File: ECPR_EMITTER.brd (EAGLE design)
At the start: 66 x 95 mm, 22 parts, among them IC1 78L05, IC2 ATMEGA8-PU, J1 0802_SCREEN, Q1 BFR96, U1 AD9850 DDS Module

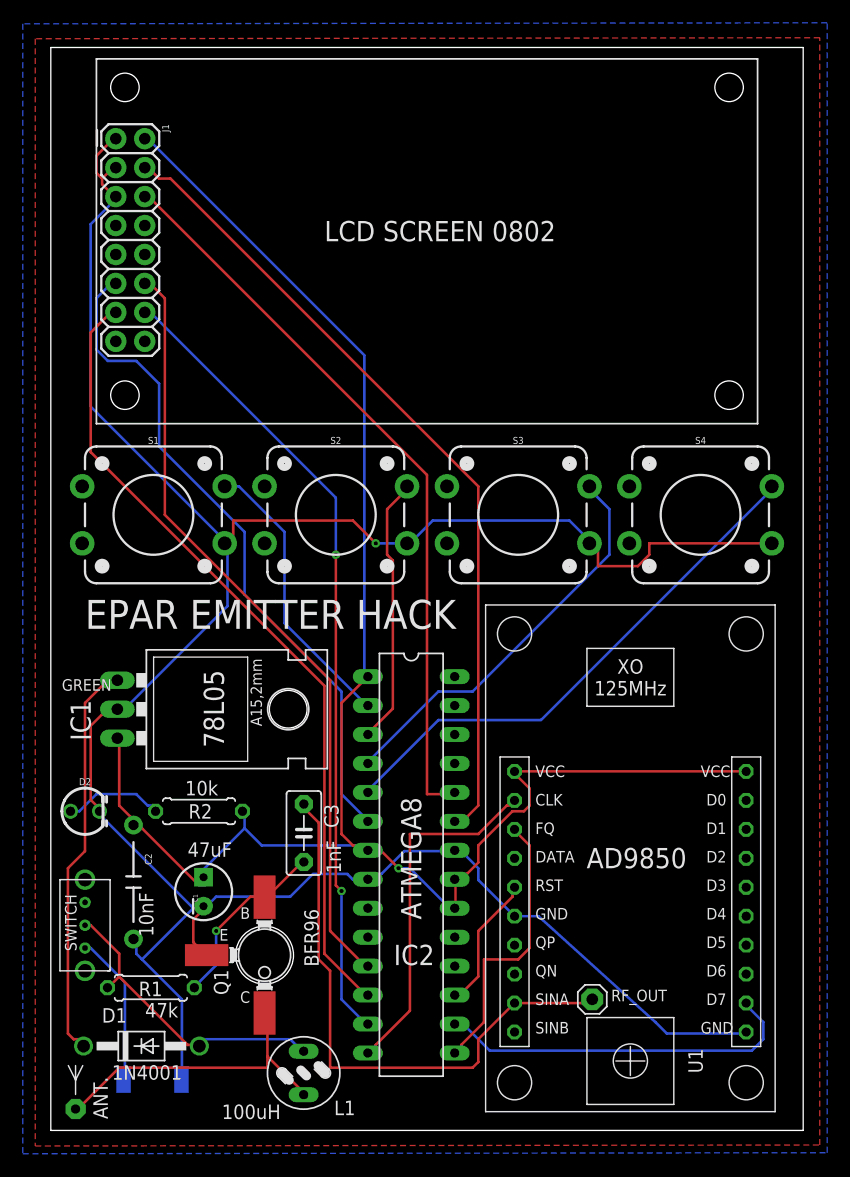
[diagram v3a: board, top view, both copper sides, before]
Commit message: feat(pcb): add rounded corners to the pcb
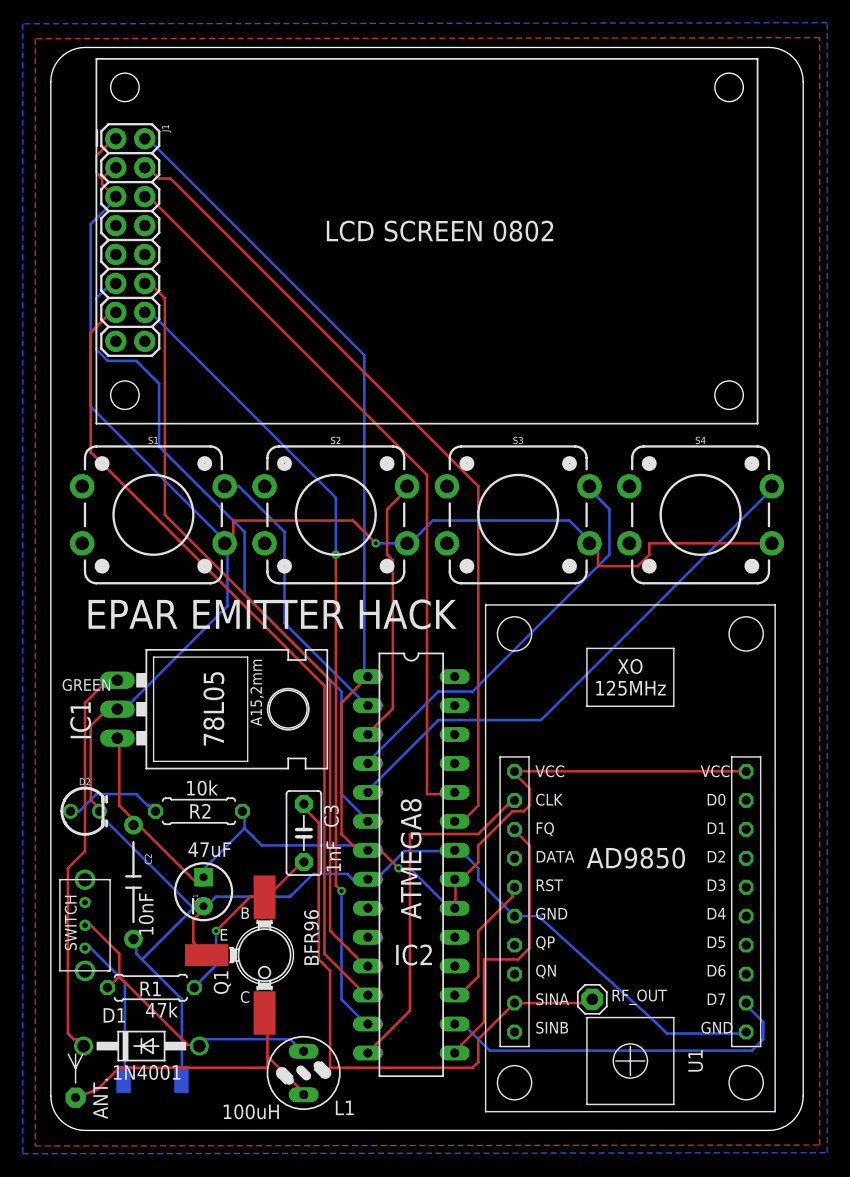
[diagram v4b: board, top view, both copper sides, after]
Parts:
- moved U$1 1.00 mm to (2.17, 2.88)
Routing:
- net N$7: track 27.8 -> 27.3 mm
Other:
- outline, holes or cut-outs redrawn
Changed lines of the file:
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@@
 <layer number="43" name="vRestrict" color="2" fill="10" visible="no" active="yes"/>
 <layer number="44" name="Drills" color="7" fill="1" visible="no" active="yes"/>
-<layer number="45" name="Holes" color="7" fill="1" visible="no" active="yes"/>
+<layer number="45" name="Holes" color="7" fill="1" visible="yes" active="yes"/>
 <layer number="46" name="Milling" color="3" fill="1" visible="no" active="yes"/>
 <layer number="47" name="Measures" color="7" fill="1" visible="no" active="yes"/>
@@
 <board>
 <plain>
-<wire x1="0" y1="0" x2="66" y2="0" width="0" layer="20"/>
-<wire x1="66" y1="0" x2="66" y2="95" width="0" layer="20"/>
-<wire x1="66" y1="95" x2="0" y2="95" width="0" layer="20"/>
-<wire x1="0" y1="95" x2="0" y2="0" width="0" layer="20"/>
 <dimension x1="4" y1="94" x2="62" y2="94" x3="33" y3="94" textsize="1.778" layer="51"/>
 <dimension x1="62" y1="94" x2="62" y2="62" x3="62" y3="78" textsize="1.778" layer="51"/>
@@
 <text x="57.5" y="28.5" size="1.016" layer="21">D0</text>
 <text x="57" y="31" size="1.016" layer="21">VCC</text>
+<wire x1="0" y1="92" x2="0" y2="3" width="0" layer="20"/>
+<wire x1="0" y1="3" x2="3" y2="0" width="0" layer="20" curve="90"/>
+<wire x1="63" y1="0" x2="66" y2="3" width="0" layer="20" curve="90"/>
+<wire x1="66" y1="3" x2="66" y2="92" width="0" layer="20"/>
+<wire x1="66" y1="92" x2="63" y2="95" width="0" layer="20" curve="90"/>
+<wire x1="63" y1="95" x2="3" y2="95" width="0" layer="20"/>
+<wire x1="3" y1="95" x2="0" y2="92" width="0" layer="20" curve="90"/>
+<wire x1="3" y1="0" x2="63" y2="0" width="0" layer="20"/>
 </plain>
 <attributes>
@@
 <attribute name="VALUE" x="57" y="47.777" size="0.6096" layer="27" font="vector" ratio="20" align="top-center"/>
 </element>
-<element name="U$1" library="computronics.com.au" package="ANTENNA" value="ANT." x="2.17" y="1.88" smashed="yes"/>
+<element name="U$1" library="computronics.com.au" package="ANTENNA" value="ANT." x="2.17" y="2.88" smashed="yes"/>
 <element name="L1" library="inductors" package="82114R" value="82114R" x="22.18" y="5.04" smashed="yes" rot="R180">
 <attribute name="NAME" x="26.72" y="2.611" size="1.27" layer="25" ratio="10" rot="R180"/>
@@
 <wire x1="22" y1="3.5" x2="22.18" y2="3.135" width="0.2286" layer="1"/>
 <wire x1="19" y1="10" x2="18.75" y2="10.3" width="0.2286" layer="1"/>
-<wire x1="6" y1="5.5" x2="2.5" y2="2" width="0.2286" layer="1"/>
+<wire x1="6" y1="5.5" x2="4.071428125" y2="3.571428125" width="0.2286" layer="1"/>
 <wire x1="19" y1="5.5" x2="6" y2="5.5" width="0.2286" layer="1"/>
 <wire x1="19" y1="6.5" x2="19" y2="5.5" width="0.2286" layer="1"/>
-<wire x1="2.5" y1="2" x2="2.17" y2="1.88" width="0.2286" layer="1"/>
+<wire x1="4.071428125" y1="3.571428125" x2="2.17" y2="2.88" width="0.2286" layer="1"/>
 </signal>
 <signal name="N$8">

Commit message: fix: screen orientation & pin23/24
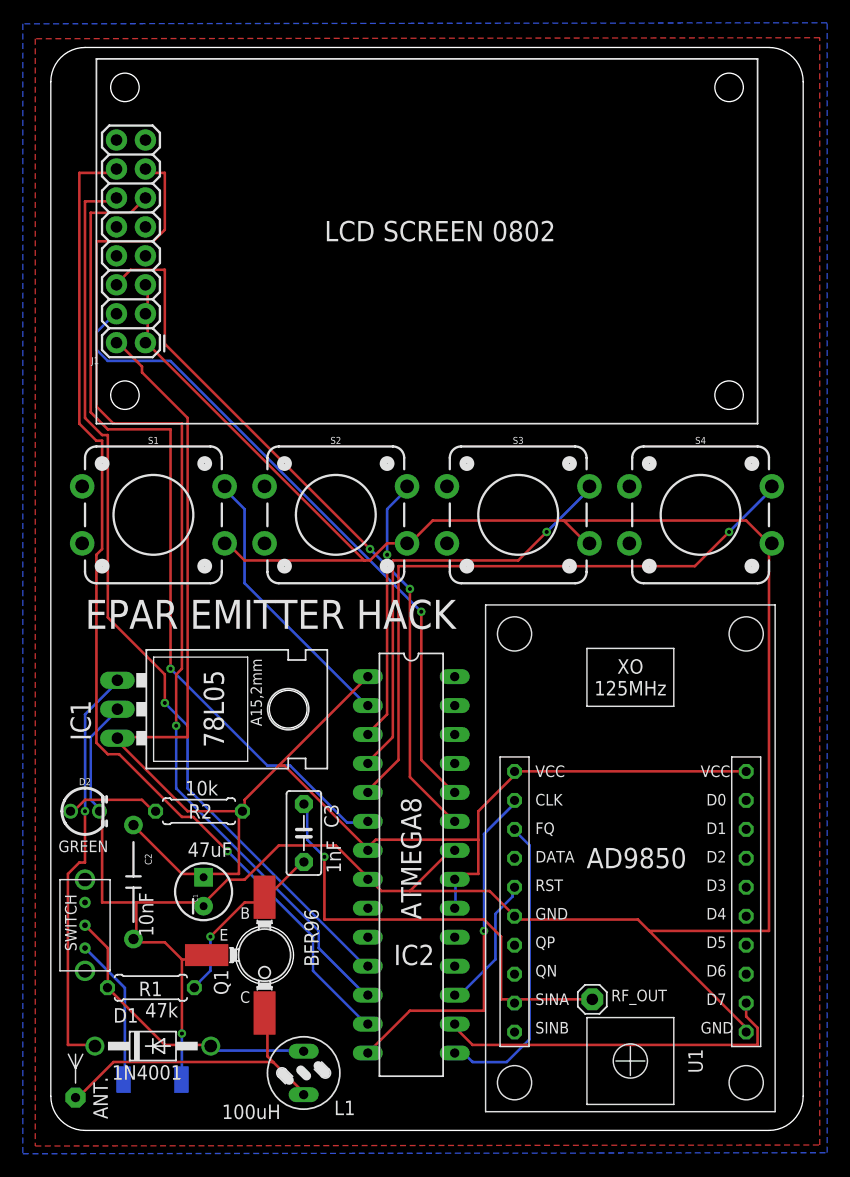
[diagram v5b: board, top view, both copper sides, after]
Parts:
- moved J1 18.1 mm to (8.30, 69.1), turned to 90 degrees
- moved D1 1.00 mm to (8.95, 7.40)
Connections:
- net N$8: now also IC2.24; no longer IC2.23
- net N$9: now also IC2.23; no longer IC2.24
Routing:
- net N$13: track 71.4 -> 93.3 mm, vias 0 -> 1
- net N$10: track 71.1 -> 90.5 mm, vias 2 -> 1
- net N$14: track 59.6 -> 74.4 mm, vias 0 -> 1
- net GND: track 227.9 -> 242.4 mm
- net N$8: track 72.0 -> 59.0 mm, vias 0 -> 1
- net N$11: track 68.5 -> 80.7 mm, vias 0 -> 1
- net N$6: track 47.1 -> 57.1 mm, vias 0 -> 1
- net RF: track 50.8 -> 40.9 mm, vias 0 -> 1
- net VCC: track 156.6 -> 147.3 mm, vias 1 -> 0
- net N$5: track 35.9 -> 39.1 mm, vias 0 -> 1
- net N$9: track 65.7 -> 63.8 mm, vias 0 -> 2
- net FQ_UD: track 25.2 -> 26.8 mm
- net VBAT: track 27.3 -> 25.8 mm
- net N$16: track 9.32 -> 8.29 mm
- net N$1: track 35.4 -> 36.4 mm, vias 0 -> 1
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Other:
- board text added: "(c) http://furrtek.free.fr/?a=epar (c) https://github.com/StoneSet/furrtek_ecpr"
- board text added: "2019 PCB designed by StoneSet - https://stoneset.fr"
- board text removed: "(c) http://furrtek.free.fr/?a=epar (c) https://github.com/StoneSet/Furrtek-Epar-ECPR"
- board text removed: "2019 PCB designed by StoneSet - https://stoneset.me"

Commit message: FUCK
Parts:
- moved J1 1.30 mm to (8.30, 70.4)
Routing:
- net GND: track 242.4 -> 220.6 mm, vias 1 -> 0
- net N$11: track 80.7 -> 91.4 mm, vias 1 -> 0
- net N$13: track 93.3 -> 83.2 mm, vias 1 -> 0
- net N$9: track 63.8 -> 73.8 mm, vias 2 -> 0
- net N$14: track 74.4 -> 64.4 mm
- net N$5: track 39.1 -> 32.5 mm, vias 1 -> 0
- net VCC: track 147.3 -> 142.7 mm
- net W_CLK: track 31.3 -> 35.0 mm, vias 1 -> 0
- net N$3: track 24.8 -> 26.9 mm
- net N$16: track 8.29 -> 10.0 mm
- net N$10: track 90.5 -> 89.0 mm
- net D7: track 31.5 -> 33.0 mm
- net N$6: track 57.1 -> 58.3 mm, vias 1 -> 0
- net N$4: track 23.5 -> 24.8 mm, vias 1 -> 0
- net VBAT: track 25.8 -> 26.9 mm
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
